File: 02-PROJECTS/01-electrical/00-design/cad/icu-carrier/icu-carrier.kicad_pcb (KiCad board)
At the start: 2 copper layers, 108 parts, among them J1 DT13-06PA, J2 backlight out, J3 DT13-12PA, J4 BT817 EVE bridge header, J5 Teensy 4.1 socket - 2 x 24 fe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, Q1 SQD50P06 class, >= 60 V, Q2 MMBT3904, SW1 IC22, U1 LMR36015FSCQ-Q1, U3 TCAN1042HVDRQ1, U4 LM393, U5 74LVC1G17, U7 LSM6DSO / ICM-42688-P, U8 XIAO ESP32C3

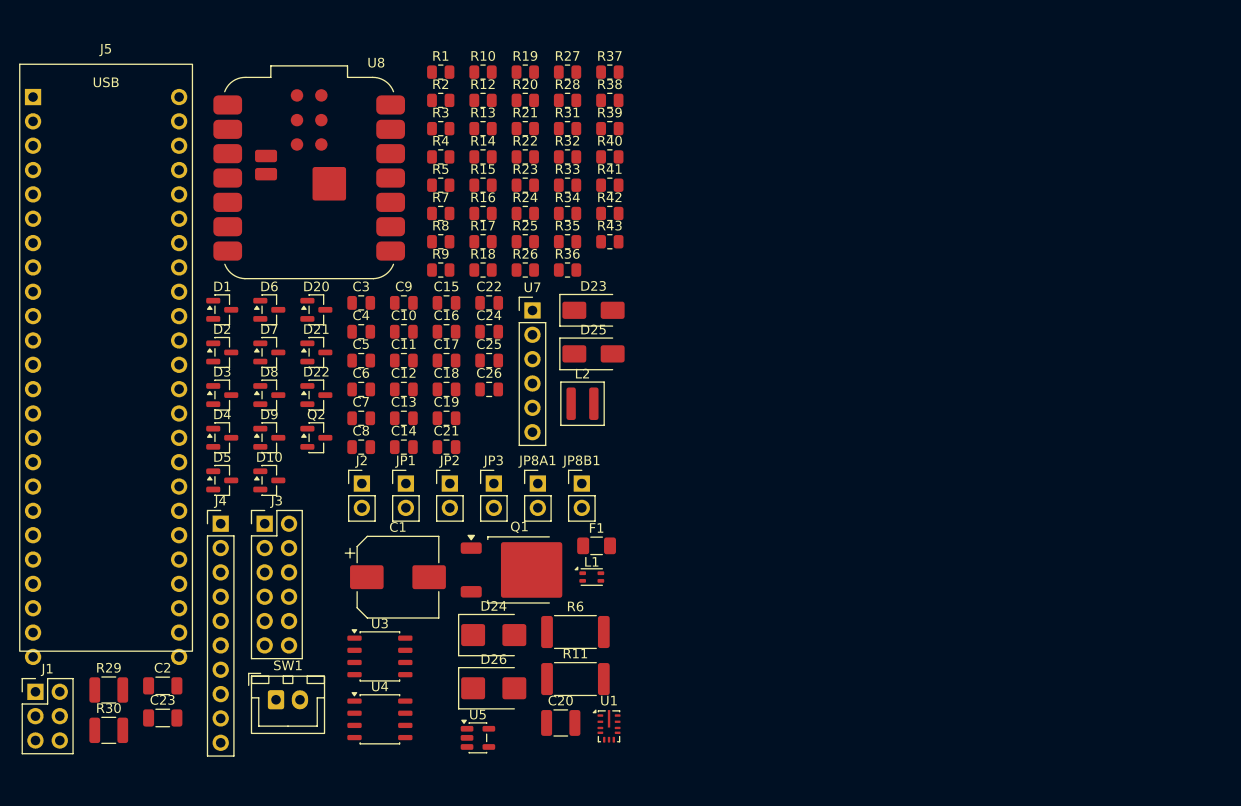
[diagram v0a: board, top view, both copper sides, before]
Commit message: Electrical: the ICU carrier's provisional board - placed, routed, poured, DRC clean, 3D complete, STEP built (F9, F10)
110 x 80 mm provisional outline (confirm until C4 / F11); DT13-06PA / 12PA footprints from TE 114-151046; the XIAO on castellations 1-14 in 1x7 sockets, EN as a P-FET power-cycle; freerouting plus a grid router, 0 unrouted; GND poured both sides; DRC 0/0/0, ERC 0/0, check.py 0 mismatches; every footprint modelled, vendor models through RX7_MODELS. Parts P169 / P109 / P176, IC24, CK25; rows F9, F10.

Co-Authored-By: Claude Fable 5.1 <noreply@anthropic.com>
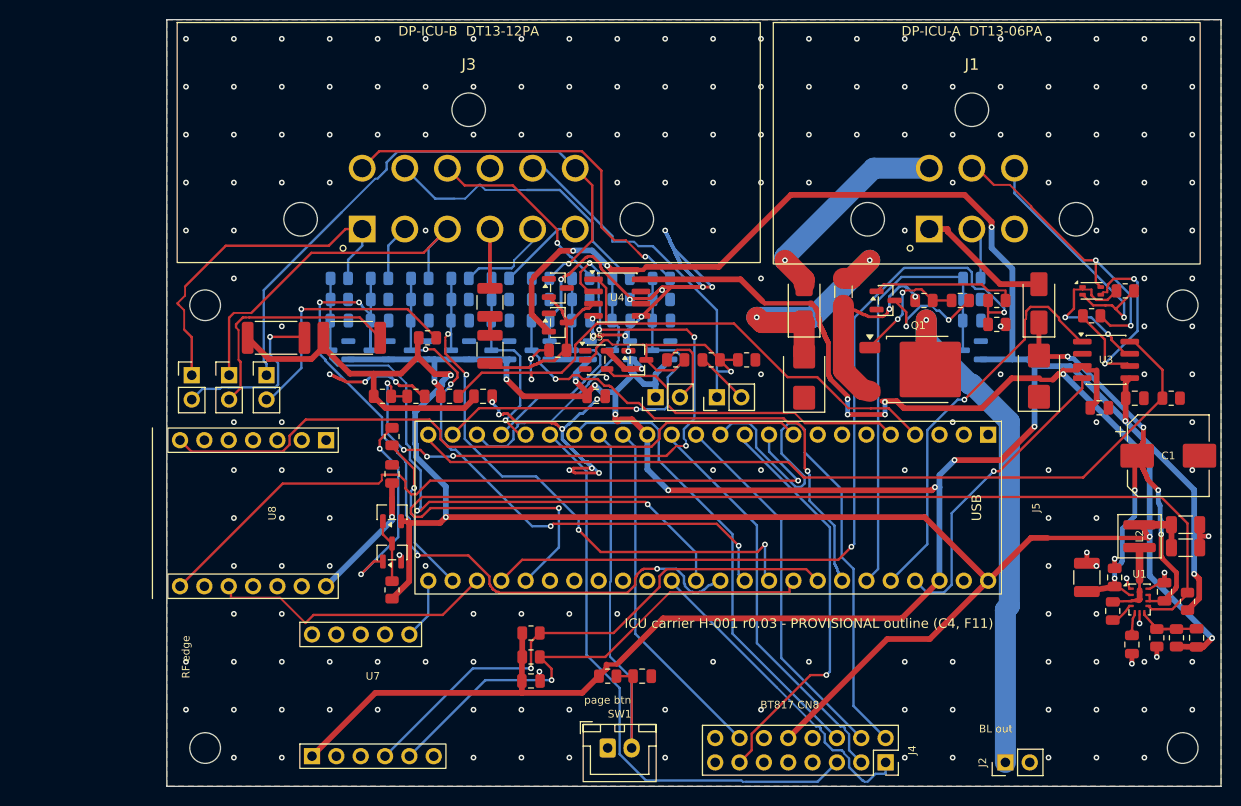
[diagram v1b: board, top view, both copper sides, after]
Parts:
- added H1: M3 - confirm at C4/F11, MountingHole:MountingHole_3.2mm_M3, F.Cu at (104.0, 79.8)
- added H2: M3 - confirm at C4/F11, MountingHole:MountingHole_3.2mm_M3, F.Cu at (206.0, 79.8)
- added H3: M3 - confirm at C4/F11, MountingHole:MountingHole_3.2mm_M3, F.Cu at (104.0, 126.0)
- added H4: M3 - confirm at C4/F11, MountingHole:MountingHole_3.2mm_M3, F.Cu at (206.0, 126.0)
- added Q3: DMG3415U class P-FET, SOT-23 - confirm, Package_TO_SOT_SMD:SOT-23, F.Cu at (123.5, 101.4)
- added Q4: MMBT3904, Package_TO_SOT_SMD:SOT-23, F.Cu at (123.5, 105.6)
- added R44: 0R, Resistor_SMD:R_0805_2012Metric, F.Cu at (200.0, 78.3)
- added R45: 0R, Resistor_SMD:R_0805_2012Metric, F.Cu at (196.5, 80.9)
- added R46: 10k, Resistor_SMD:R_0805_2012Metric, F.Cu at (123.5, 109.5)
- added R47: 10k, Resistor_SMD:R_0805_2012Metric, F.Cu at (123.5, 93.5)
- C10, C11, C12, C13, C14, C5, C6, C7, C8, C9, D1, D10, D2, D3, D4, D5, D6, D7, D8, D9, R10, R12, R13, R14, R15, R16, R17, R19, R20, R21, R22, R23, R24, R25, R26, R27, R28, R7, R8, R9: moved to B.Cu
- J1: footprint Connector_PinHeader_2.54mm:PinHeader_2x03_P2.54mm_Vertical -> icu-carrier:DT13-06PA
- J3: footprint Connector_PinHeader_2.54mm:PinHeader_2x06_P2.54mm_Vertical -> icu-carrier:DT13-12PA
- J4: value BT817 EVE bridge header -> ME817EV CN8 - 2x8 host header, JP1 2-3 (5 V from this board); footprint Connector_PinHeader_2.54mm:PinHeader_1x10_P2.54mm_Vertical -> Connector_PinSocket_2.54mm:PinSocket_2x08_P2.54mm_Vertical
- L1: value common-mode choke - DNP -> common-mode choke - DNP; fit only with R44 / R45 removed
- U3, U4: footprint Package_SO:JEITA_SOIC-8_3.9x4.9mm_P1.27mm -> Package_SO:SOIC-8_3.9x4.9mm_P1.27mm
- U7: value LSM6DSO / ICM-42688-P -> Adafruit 4517 LSM6DSOX+LIS3MDL (LSM6DSO class, P109 - confirm the board bought); footprint Connector_PinHeader_2.54mm:PinHeader_1x06_P2.54mm_Vertical -> icu-carrier:IMU_Adafruit_4517_Socket
- U8: value XIAO ESP32C3 -> XIAO ESP32C3 2x7 socket (Seeed, S-490); footprint RF_Module:MCU_Seeed_ESP32C3 -> icu-carrier:XIAO_ESP32C3_Socket_2x07
- moved J1 110.4 mm to (184.0, 68.7)
- moved C23 108.6 mm to (206.3, 102.7)
- moved C2 107.7 mm to (206.3, 105.1)
- moved J5 105.7 mm to (185.7, 93.3), turned to -90 degrees
- moved U3 81.8 mm to (198.0, 85.5)
- moved C1 81.4 mm to (204.5, 95.5)
- moved C4 81.0 mm to (201.0, 89.5)
- moved R5 79.4 mm to (204.8, 89.5)
- moved C26 78.2 mm to (207.4, 114.5), turned to 90 degrees
- moved C3 77.8 mm to (197.3, 90.5)
- moved C22 76.6 mm to (204.1, 109.7), turned to 90 degrees
- moved R41 75.7 mm to (205.3, 114.5), turned to 90 degrees
- moved D10 74.6 mm to (184.0, 84.5), turned to 180 degrees
- moved J4 73.7 mm to (175.0, 127.5), turned to -90 degrees
- moved C25 73.3 mm to (200.7, 115.2), turned to -90 degrees
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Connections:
- net Net-(U3-CANH) renamed /CANH_U
- net Net-(U3-CANL) renamed /CANL_U
- C19 pad 1: +5V -> /RADIO_5V
- J4 pad 1: +3V3 -> /SPI_SCK
- J4 pad 10: /BT817_PD -> +5V
- J4 pad 2: GND -> /SPI_CS
- J4 pad 3: /SPI_CS -> /SPI_MISO
- J4 pad 4: /SPI_SCK -> /SPI_MOSI
- J4 pad 5: /SPI_MOSI -> /BT_IO3
- J4 pad 6: /SPI_MISO -> /BT_IO2
- J4 pad 7: /BT_IO2 -> unconnected-(J4-NC-Pad7)
- J4 pad 8: /BT_IO3 -> unconnected-(J4-NC-Pad8)
- J4 pad 9: /BT817_INT -> unconnected-(J4-NC-Pad9)
- U7 pad 2: GND -> unconnected-(U7-3Vo-Pad2)
- U7 pad 3: /I2C_SCL -> GND
- U7 pad 4: /I2C_SDA -> /I2C_SCL
- U7 pad 5: /IMU_INT -> /I2C_SDA
- U7 pad 6: (no net) -> unconnected-(U7-INT2-Pad6)
- U8 pad 1: +5V -> unconnected-(U8-D0/A0-Pad1)
- U8 pad 10: (no net) -> /RADIO_BOOT
- U8 pad 11: (no net) -> unconnected-(U8-D10/MOSI-Pad11)
- U8 pad 12: (no net) -> unconnected-(U8-3V3_OUT-Pad12)
- U8 pad 13: (no net) -> GND
- U8 pad 14: (no net) -> /RADIO_5V
- U8 pad 2: GND -> unconnected-(U8-D1/A1-Pad2)
- U8 pad 4: /RADIO_TX -> unconnected-(U8-D3/A3-Pad4)
- U8 pad 5: /RADIO_RX -> unconnected-(U8-D4/SDA-Pad5)
- U8 pad 6: /RADIO_EN -> unconnected-(U8-D5/SCL-Pad6)
- U8 pad 7: /RADIO_BOOT -> /RADIO_TX
- U8 pad 8: unconnected-(U8-ANT-Pad8) -> /RADIO_RX
- U8 pad 9: (no net) -> unconnected-(U8-D8/SCK-Pad9)
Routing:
- net +3V3: track 0.00 -> 335.6 mm, vias 0 -> 15
- net +5V: track 0.00 -> 292.0 mm, vias 0 -> 9
- net GND: track 0.00 -> 149.0 mm, vias 0 -> 206
- net /PG_5V: track 0.00 -> 120.4 mm, vias 0 -> 1
- net /CAN_STB: track 0.00 -> 89.8 mm
- net /BL_EN: track 0.00 -> 87.0 mm, vias 0 -> 2
- net /IC02_ADC: track 0.00 -> 85.2 mm, vias 0 -> 4
- net /RADIO_RX: track 0.00 -> 77.6 mm, vias 0 -> 1
- net Net-(U4A--): track 0.00 -> 74.9 mm, vias 0 -> 8
- net /RADIO_TX: track 0.00 -> 70.2 mm
- net /IC04_CAP: track 0.00 -> 67.0 mm, vias 0 -> 2
- net /IC01_ADC: track 0.00 -> 66.0 mm, vias 0 -> 2
- net /ICU_B7: track 0.00 -> 63.0 mm, vias 0 -> 1
- net /ICU_B8: track 0.00 -> 62.4 mm, vias 0 -> 1
- net /BT_IO3: track 0.00 -> 61.1 mm
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- added copper zone on B.Cu, net GND
- added copper zone on F.Cu, net GND
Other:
- board outline added: 110 x 80 mm
- board text added: "BL out"
- board text added: "BT817 CN8"
- board text added: "DP-ICU-A DT13-06PA"
- board text added: "DP-ICU-B DT13-12PA"
- board text added: "ICU carrier H-001 r0.03 - PROVISIONAL outline (C4, F11)"
- board text added: "RF edge"
- board text added: "front ends IC01-IC11, IC14: R / R / 100n / BAT54S on this side"
- board text added: "page btn"
